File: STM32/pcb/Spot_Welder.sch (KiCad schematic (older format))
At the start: 34 parts, among them J1 SSD1306, J5 Battery, J6 Foot_Switch, SW1 RE, U2 STM32F030F4Px, U3 AMS1117-3.3, U4 ZXGD3009E6

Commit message: pcb update
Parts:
- added C1: 10u, Capacitor_SMD:C_0805_2012Metric, symbol Device:C
- added H3, H4, H5, H6: MountingHole, MountingHole:MountingHole_2.5mm, symbol Mechanical:MountingHole
- added R21, R22: 4.7k, Resistor_SMD:R_0603_1608Metric, symbol Device:R
- C6: value 1u -> 10u; footprint Capacitor_SMD:C_0603_1608Metric -> Capacitor_SMD:C_0805_2012Metric
- C7: value 1u -> 22u; footprint Capacitor_SMD:C_0603_1608Metric -> Capacitor_SMD:C_1206_3216Metric
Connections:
- net 3.3V_MCU: now also C1.1, R21.1, R22.1
- net GND: now also U3.1 (GND), C1.2
- net SCL: now also R21.2
- net SDA: now also R22.2
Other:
- moved on the sheet: U2
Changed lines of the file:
@@
 EESchema Schematic File Version 5
-LIBS:Spot_Welder-cache
 EELAYER 30 0
 EELAYER END
@@
 Comment3 ""
 Comment4 ""
+Comment5 ""
+Comment6 ""
+Comment7 ""
+Comment8 ""
+Comment9 ""
 $EndDescr
 $Comp
 L MCU_ST_STM32F0:STM32F030F4Px U2
 U 1 1 5D58381A
-P 3100 5100
-F 0 "U2" H 3100 4211 50  0000 C CNN
-F 1 "STM32F030F4Px" H 3100 4120 50  0000 C CNN
-F 2 "Package_SO:TSSOP-20_4.4x6.5mm_P0.65mm" H 2700 4400 50  0001 R CNN
-F 3 "http://www.st.com/st-web-ui/static/active/en/resource/technical/document/datasheet/DM00088500.pdf" H 3100 5100 50  0001 C CNN
-	1    3100 5100
+P 4100 6000
+F 0 "U2" H 4100 5111 50  0000 C CNN
+F 1 "STM32F030F4Px" H 4100 5020 50  0000 C CNN
+F 2 "Package_SO:TSSOP-20_4.4x6.5mm_P0.65mm" H 3700 5300 50  0001 R CNN
+F 3 "http://www.st.com/st-web-ui/static/active/en/resource/technical/document/datasheet/DM00088500.pdf" H 4100 6000 50  0001 C CNN
+	1    4100 6000
 	1    0    0    -1
 $EndComp
@@
 P 4350 1350
 F 0 "C6" H 4236 1396 50  0000 R CNN
-F 1 "1u" H 4236 1305 50  0000 R CNN
-F 2 "Capacitor_SMD:C_0603_1608Metric" H 4388 1200 50  0001 C CNN
+F 1 "10u" H 4236 1305 50  0000 R CNN
+F 2 "Capacitor_SMD:C_0805_2012Metric" H 4388 1200 50  0001 C CNN
 F 3 "~" H 4350 1350 50  0001 C CNN
 	1    4350 1350
@@
 P 5350 1350
 F 0 "C7" H 5236 1396 50  0000 R CNN
-F 1 "1u" H 5236 1305 50  0000 R CNN
-F 2 "Capacitor_SMD:C_0603_1608Metric" H 5388 1200 50  0001 C CNN
+F 1 "22u" H 5236 1305 50  0000 R CNN
+F 2 "Capacitor_SMD:C_1206_3216Metric" H 5388 1200 50  0001 C CNN
 F 3 "~" H 5350 1350 50  0001 C CNN
 	1    5350 1350
@@
 	4350 1500 4350 1650
 Wire Wire Line
-	5350 1650 5350 1500
+	5350 1650 5350 1600
 Text GLabel 4350 950  1    50   Input ~ 0
 12V_VCC
@@
 	1    0    0    -1
 $EndComp
-Text GLabel 4650 2350 0    50   Input ~ 0
-3.3V_MCU
-Wire Wire Line
-	4650 2350 4750 2350
-Wire Wire Line
-	4750 2350 4750 2550
-Wire Wire Line
-	4750 2550 4800 2550
-$Comp
-L power:GND #PWR0101
-U 1 1 5D78F79B
-P 4300 2750
-F 0 "#PWR0101" H 4300 2500 50  0001 C CNN
-F 1 "GND" H 4305 2577 50  0000 C CNN
-F 2 "" H 4300 2750 50  0001 C CNN
-F 3 "" H 4300 2750 50  0001 C CNN
-	1    4300 2750
-	1    0    0    -1
-$EndComp
-Wire Wire Line
-	4300 2750 4300 2650
-Wire Wire Line
-	4300 2650 4800 2650
-Text GLabel 4700 2750 0    50   Input ~ 0
-SCL
-Text GLabel 4700 2850 0    50   Input ~ 0
+Text GLabel 4100 2850 0    50   Input ~ 0
 SDA
 Wire Wire Line
-	4700 2750 4800 2750
-Wire Wire Line
-	4700 2850 4800 2850
+	4100 2850 4450 2850
 Wire Notes Line
 	5700 1950 5700 3500
@@
 F1 "MOSFET_Array.sch" 50
 $EndSheet
+$Comp
+L power:GND #PWR0105
+U 1 1 5D9385C4
+P 4850 1700
+F 0 "#PWR0105" H 4850 1450 50  0001 C CNN
+F 1 "GND" H 4855 1527 50  0000 C CNN
+F 2 "" H 4850 1700 50  0001 C CNN
+F 3 "" H 4850 1700 50  0001 C CNN
+	1    4850 1700
+	1    0    0    -1
+$EndComp
+Wire Wire Line
+	4850 1700 4850 1350
+$Comp
+L Mechanical:MountingHole H3
+U 1 1 5D9367B8
+P 1300 2550
+F 0 "H3" H 1400 2596 50  0000 L CNN
+F 1 "MountingHole" H 1400 2505 50  0000 L CNN
+F 2 "MountingHole:MountingHole_2.5mm" H 1300 2550 50  0001 C CNN
+F 3 "~" H 1300 2550 50  0001 C CNN
+	1    1300 2550
+	1    0    0    -1
+$EndComp
+$Comp
+L Mechanical:MountingHole H4
+U 1 1 5D937A6C
+P 1300 2800
+F 0 "H4" H 1400 2846 50  0000 L CNN
+F 1 "MountingHole" H 1400 2755 50  0000 L CNN
+F 2 "MountingHole:MountingHole_2.5mm" H 1300 2800 50  0001 C CNN
+F 3 "~" H 1300 2800 50  0001 C CNN
+	1    1300 2800
+	1    0    0    -1
+$EndComp
+$Comp
+L Mechanical:MountingHole H5
+U 1 1 5D9397FA
+P 1300 3050
+F 0 "H5" H 1400 3096 50  0000 L CNN
+F 1 "MountingHole" H 1400 3005 50  0000 L CNN
+F 2 "MountingHole:MountingHole_2.5mm" H 1300 3050 50  0001 C CNN
+F 3 "~" H 1300 3050 50  0001 C CNN
+	1    1300 3050
+	1    0    0    -1
+$EndComp
+$Comp
+L Mechanical:MountingHole H6
+U 1 1 5D93AEBC
+P 1300 3300
+F 0 "H6" H 1400 3346 50  0000 L CNN
+F 1 "MountingHole" H 1400 3255 50  0000 L CNN
+F 2 "MountingHole:MountingHole_2.5mm" H 1300 3300 50  0001 C CNN
+F 3 "~" H 1300 3300 50  0001 C CNN
+	1    1300 3300
+	1    0    0    -1
+$EndComp
+$Comp
+L Device:C C1
+U 1 1 5DA83E12
+P 5600 1350
+F 0 "C1" H 5500 1450 50  0000 R CNN
+F 1 "10u" H 5550 1200 50  0000 R CNN
+F 2 "Capacitor_SMD:C_0805_2012Metric" H 5638 1200 50  0001 C CNN
+F 3 "~" H 5600 1350 50  0001 C CNN
+	1    5600 1350
+	1    0    0    -1
+$EndComp
+Wire Wire Line
+	5600 1200 5600 1050
+Wire Wire Line
+	5600 1050 5350 1050
+Wire Wire Line
+	5600 1500 5600 1600
+Wire Wire Line
+	5600 1600 5350 1600
+Connection ~ 5350 1600
+Wire Wire Line
+	5350 1600 5350 1500
+Wire Wire Line
+	4100 2750 4200 2750
+Text GLabel 4100 2750 0    50   Input ~ 0
+SCL
+Wire Wire Line
+	4300 2650 4800 2650
+Wire Wire Line
+	4300 3150 4300 2650
+$Comp
+L power:GND #PWR0101
+U 1 1 5D78F79B
+P 4300 3150
+F 0 "#PWR0101" H 4300 2900 50  0001 C CNN
+F 1 "GND" H 4305 2977 50  0000 C CNN
+F 2 "" H 4300 3150 50  0001 C CNN
+F 3 "" H 4300 3150 50  0001 C CNN
+	1    4300 3150
+	1    0    0    -1
+$EndComp
+Wire Wire Line
+	4750 2550 4800 2550
+Wire Wire Line
+	4750 2200 4750 2550
+Wire Wire Line
+	4350 2200 4450 2200
+Text GLabel 4350 2200 0    50   Input ~ 0
+3.3V_MCU
+$Comp
+L Device:R R21
+U 1 1 5DAFE2BC
+P 4200 2450
+F 0 "R21" H 4130 2496 50  0000 R CNN
+F 1 "4.7k" H 4130 2405 50  0000 R CNN
+F 2 "Resistor_SMD:R_0603_1608Metric" V 4130 2450 50  0001 C CNN
+F 3 "~" H 4200 2450 50  0001 C CNN
+	1    4200 2450
+	1    0    0    -1
+$EndComp
+$Comp
+L Device:R R22
+U 1 1 5DB04CA4
+P 4450 2450
+F 0 "R22" H 4600 2500 50  0000 R CNN
+F 1 "4.7k" H 4700 2400 50  0000 R CNN
+F 2 "Resistor_SMD:R_0603_1608Metric" V 4380 2450 50  0001 C CNN
+F 3 "~" H 4450 2450 50  0001 C CNN
+	1    4450 2450
+	1    0    0    -1
+$EndComp
+Wire Wire Line
+	4200 2600 4200 2750
+Connection ~ 4200 2750
+Wire Wire Line
+	4200 2750 4800 2750
+Wire Wire Line
+	4450 2600 4450 2850
+Connection ~ 4450 2850
+Wire Wire Line
+	4450 2850 4800 2850
+Wire Wire Line
+	4450 2300 4200 2300
+Wire Wire Line
+	4450 2300 4450 2200
+Connection ~ 4450 2300
+Connection ~ 4450 2200
+Wire Wire Line
+	4450 2200 4750 2200
 $EndSCHEMATC

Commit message: pcb complete
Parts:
- added C14, C15: 0.1u, Capacitor_SMD:C_0603_1608Metric, symbol Device:C
- added C2: 1u, Capacitor_SMD:C_0603_1608Metric, symbol Device:C
- added FB1: Ferrite_Bead, Inductor_SMD:L_0603_1608Metric, symbol Device:Ferrite_Bead
- added J2: Debug, Connector_PinSocket_2.54mm:PinSocket_1x03_P2.54mm_Vertical, symbol Connector_Generic:Conn_01x03
- added R23: 10k, Resistor_SMD:R_0603_1608Metric, symbol Device:R
- added U12: AT24CS04-STUM, Package_TO_SOT_SMD:SOT-23-5, symbol Memory_EEPROM:AT24CS04-STUM
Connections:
- net 3.3V_MCU: now also U2.16 (VDD), C14.1, FB1.1, R23.2, U12.4 (VCC)
- net ADC_Pulse: now also U2.6 (PA0)
- net ADC_VIN: now also U2.11 (PA5)
- net Encoder_A: now also U2.12 (PA6)
- net Encoder_B: now also U2.13 (PA7)
- net Encoder_Switch: now also U2.14 (PB1)
- net Foot_Switch: now also U2.10 (PA4)
- net GND: now also U2.1 (BOOT0), U2.15 (VSS), C14.2, C15.2, C2.2, J2.3 (Pin_3), U12.2 (GND), U12.5 (WP)
- net MCU_Gate: now also U2.7 (PA1)
- net SCL: now also U2.17 (PA9), U12.1 (SCL)
- net SDA: now also U2.18 (PA10), U12.3 (SDA)
- net SWDIO: now reaches U2.19 (PA13)
- net SWDIO: now also J2.1 (Pin_1)
- net SWCLK: now reaches U2.20 (PA14)
- net SWCLK: now also J2.2 (Pin_2)
- net at U2.4 (NRST): now also C2.1, R23.1
- net VDDA: now reaches U2.5 (VDDA)
- net VDDA: now also C15.1, FB1.2
- no-connect marks 0 -> 4
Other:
- note added: "EEPROM"
- note added: "OLED"
- note added: "Power Flags"
- moved on the sheet: H3, H4, H5, H6

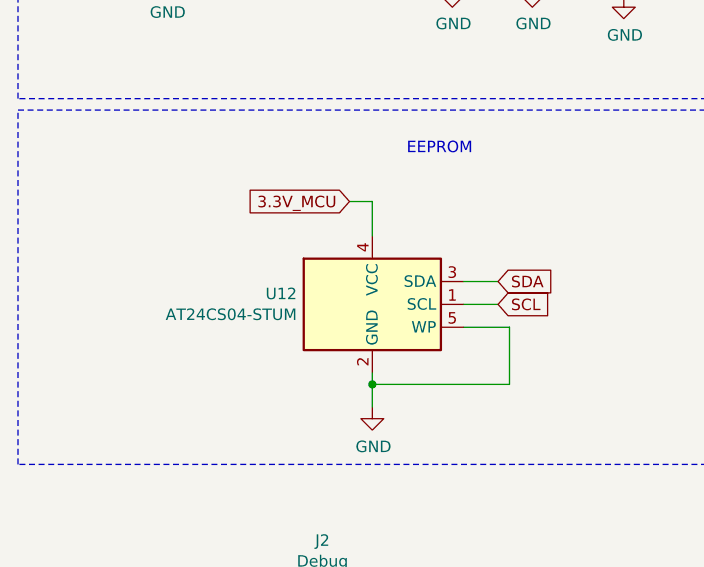
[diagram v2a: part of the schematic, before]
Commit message: eeprom footprint changed
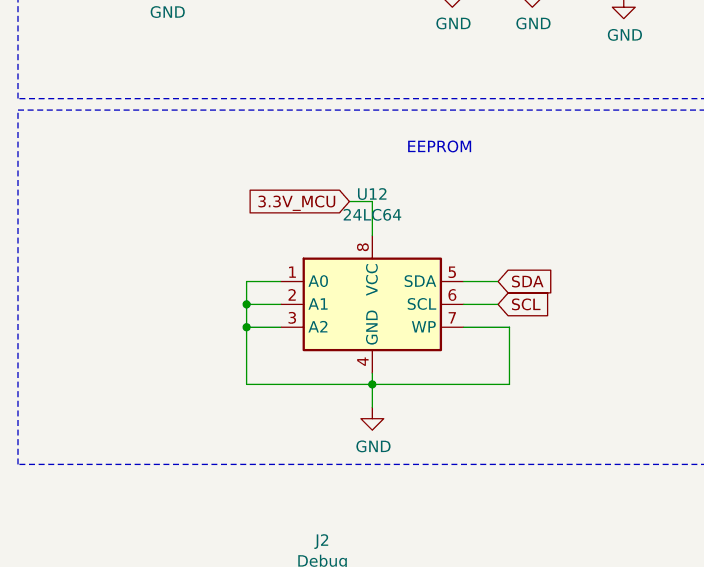
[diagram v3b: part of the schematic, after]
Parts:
- removed U12: AT24CS04-STUM, Package_TO_SOT_SMD:SOT-23-5, symbol Memory_EEPROM:AT24CS04-STUM
- added U12: 24LC64, Package_SO:TSSOP-8_4.4x3mm_P0.65mm, symbol Memory_EEPROM:24LC64
- C7: footprint Capacitor_SMD:C_1206_3216Metric -> Capacitor_SMD:C_0805_2012Metric
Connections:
- net 3.3V_MCU: now also U12.8 (VCC)
- net GND: now also U12.1 (A0), U12.2 (A1), U12.3 (A2), U12.4 (GND), U12.7 (WP)
- net SCL: now also U12.6 (SCL)
- net SDA: now also U12.5 (SDA)
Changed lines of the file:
@@
 F 0 "C7" H 5236 1396 50  0000 R CNN
 F 1 "22u" H 5236 1305 50  0000 R CNN
-F 2 "Capacitor_SMD:C_1206_3216Metric" H 5388 1200 50  0001 C CNN
+F 2 "Capacitor_SMD:C_0805_2012Metric" H 5388 1200 50  0001 C CNN
 F 3 "~" H 5350 1350 50  0001 C CNN
 	1    5350 1350
@@
 Wire Wire Line
 	4450 2200 4750 2200
-$Comp
-L Memory_EEPROM:AT24CS04-STUM U12
-U 1 1 5D95BB2E
-P 2050 2800
-F 0 "U12" H 1720 2846 50  0000 R CNN
-F 1 "AT24CS04-STUM" H 1720 2755 50  0000 R CNN
-F 2 "Package_TO_SOT_SMD:SOT-23-5" H 2050 2800 50  0001 C CNN
-F 3 "http://ww1.microchip.com/downloads/en/DeviceDoc/Atmel-8766-SEEPROM-AT24CS04-08-Datasheet.pdf" H 2050 2800 50  0001 C CNN
-	1    2050 2800
-	1    0    0    -1
-$EndComp
 Text GLabel 2600 2800 2    50   Input ~ 0
 SCL
@@
 NoConn ~ 4850 5800
 NoConn ~ 4850 5700
+$Comp
+L Memory_EEPROM:24LC64 U12
+U 1 1 5DA8B716
+P 2050 2800
+F 0 "U12" H 2050 3281 50  0000 C CNN
+F 1 "24LC64" H 2050 3190 50  0000 C CNN
+F 2 "Package_SO:TSSOP-8_4.4x3mm_P0.65mm" H 2050 2800 50  0001 C CNN
+F 3 "http://ww1.microchip.com/downloads/en/DeviceDoc/21189f.pdf" H 2050 2800 50  0001 C CNN
+	1    2050 2800
+	1    0    0    -1
+$EndComp
+Wire Wire Line
+	1650 2700 1500 2700
+Wire Wire Line
+	1500 2700 1500 2800
+Wire Wire Line
+	1500 3150 2050 3150
+Wire Wire Line
+	1650 2900 1500 2900
+Connection ~ 1500 2900
+Wire Wire Line
+	1500 2900 1500 3150
+Wire Wire Line
+	1650 2800 1500 2800
+Connection ~ 1500 2800
+Wire Wire Line
+	1500 2800 1500 2900
 $EndSCHEMATC

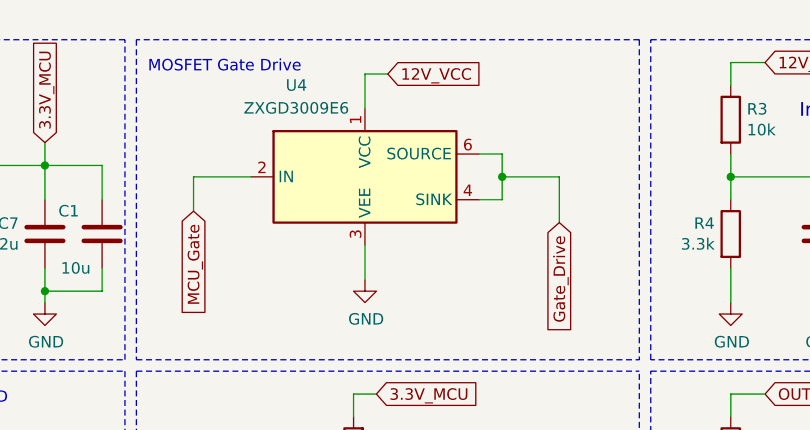
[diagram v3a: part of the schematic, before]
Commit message: gate driver changed to mcp1416
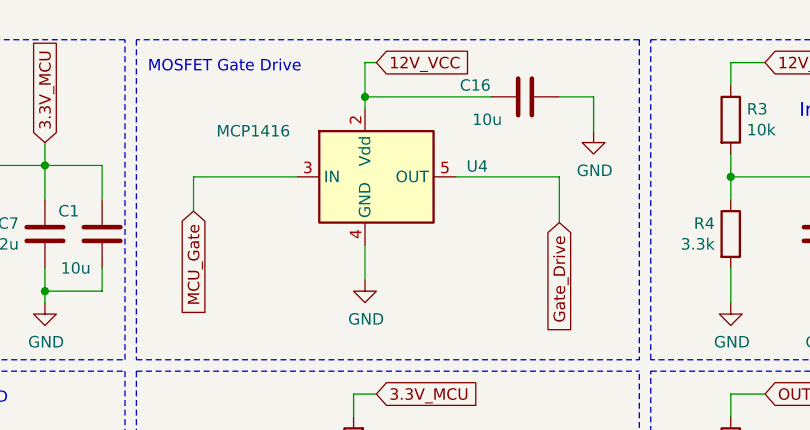
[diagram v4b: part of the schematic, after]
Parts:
- removed U4: ZXGD3009E6, Package_TO_SOT_SMD:SOT-23-6, symbol Driver_FET:ZXGD3009E6
- added C16: 10u, Capacitor_SMD:C_0805_2012Metric, symbol Device:C
- added U4: MCP1416, Package_TO_SOT_SMD:SOT-23-5, symbol Driver_FET:MCP1416
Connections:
- net 12V_VCC: now also C16.2, U4.2 (Vdd)
- net GND: now also C16.1, U4.4 (GND)
- net Gate_Drive: now also U4.5 (OUT)
- net MCU_Gate: now also U4.3 (IN)
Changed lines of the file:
@@
 	5700 500  3900 500
-$Comp
-L Driver_FET:ZXGD3009E6 U4
-U 1 1 5D633BA2
-P 6750 1100
-F 0 "U4" H 6450 1500 50  0000 C CNN
-F 1 "ZXGD3009E6" H 6450 1400 50  0000 C CNN
-F 2 "Package_TO_SOT_SMD:SOT-23-6" H 6750 600 50  0001 C CNN
-F 3 "https://www.diodes.com/assets/Datasheets/ZXGD3009E6.pdf" H 6400 1350 50  0001 C CNN
-	1    6750 1100
-	1    0    0    -1
-$EndComp
 $Comp
 L power:GND #PWR010
@@
 Wire Wire Line
 	6750 1400 6750 1550
-Text GLabel 6850 650  2    50   Input ~ 0
-12V_VCC
-Wire Wire Line
-	6850 650  6750 650
-Wire Wire Line
-	6750 650  6750 800
 Wire Notes Line
 	5750 500  5750 1900
-Wire Wire Line
-	7250 1000 7350 1000
-Wire Wire Line
-	7350 1000 7350 1100
-Wire Wire Line
-	7350 1200 7250 1200
 Text GLabel 6000 1250 3    50   Input ~ 0
 MCU_Gate
 Wire Wire Line
 	6000 1250 6000 1100
-Wire Wire Line
-	6000 1100 6250 1100
 Wire Notes Line
 	7950 500  7950 1900
@@
 Wire Wire Line
 	7600 1300 7600 1100
-Wire Wire Line
-	7600 1100 7350 1100
-Connection ~ 7350 1100
-Wire Wire Line
-	7350 1100 7350 1200
 $Sheet
 S 6400 3800 1200 450
@@
 Wire Wire Line
 	1500 2800 1500 2900
+$Comp
+L Driver_FET:MCP1416 U4
+U 1 1 5DD08CA7
+P 6750 1100
+F 0 "U4" H 7194 1146 50  0000 L CNN
+F 1 "MCP1416" H 6100 1300 50  0000 L CNN
+F 2 "Package_TO_SOT_SMD:SOT-23-5" H 6750 700 50  0001 C CIN
+F 3 "http://ww1.microchip.com/downloads/en/DeviceDoc/20002092F.pdf" H 6550 1350 50  0001 C CNN
+	1    6750 1100
+	1    0    0    -1
+$EndComp
+Wire Wire Line
+	6000 1100 6450 1100
+Wire Wire Line
+	7150 1100 7600 1100
+Text GLabel 6800 600  2    50   Input ~ 0
+12V_VCC
+Wire Wire Line
+	6800 600  6750 600
+Wire Wire Line
+	6750 600  6750 750
+Wire Wire Line
+	6750 750  7300 750
+Connection ~ 6750 750
+Wire Wire Line
+	6750 750  6750 800
+$Comp
+L power:GND #PWR0116
+U 1 1 5DD265CC
+P 7750 900
+F 0 "#PWR0116" H 7750 650 50  0001 C CNN
+F 1 "GND" H 7755 727 50  0000 C CNN
+F 2 "" H 7750 900 50  0001 C CNN
+F 3 "" H 7750 900 50  0001 C CNN
+	1    7750 900
+	1    0    0    -1
+$EndComp
+Wire Wire Line
+	7750 900  7750 750
+Wire Wire Line
+	7750 750  7600 750
+$Comp
+L Device:C C16
+U 1 1 5DD18B9A
+P 7450 750
+F 0 "C16" V 7400 600 50  0000 R CNN
+F 1 "10u" V 7550 650 50  0000 R CNN
+F 2 "Capacitor_SMD:C_0805_2012Metric" H 7488 600 50  0001 C CNN
+F 3 "~" H 7450 750 50  0001 C CNN
+	1    7450 750
+	0    1    1    0
+$EndComp
 $EndSCHEMATC
